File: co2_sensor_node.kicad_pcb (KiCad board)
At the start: 4 copper layers, 100 x 100 mm, 132 parts, among them J1 Conn_01x03, J10 Conn_01x04, J11 USB_B, J12 Conn_01x02, J13 TF-15x15, J2 Conn_01x03, J3 Conn_01x02, J4 Conn_01x02, J5 Conn_01x03, J6 Conn_01x03, J7 Conn_01x02, J8 Conn_01x02, J9 Conn_01x04, Q1 AO3400A, Q2 AO3401A, Q3 AO3401A, Q4 SS8050, Q5 SS8050, Q6 AO3400A, SW1 K2-1102SP-C4SC-04, U1 BQ24074RGT, U2 TPS62130, U3 CH340C, U4 ESP32-WROOM-32D, U5 TC1508S

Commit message: Add 5V boost converter and begin redesign of PCB
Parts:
- removed the J1 at (114.0, 103.5)
- removed the J11 at (175.2, 67.1)
- removed J12: Conn_01x02, co2_sensor_node:KF301-5.0-2P
- removed the J2 at (114.0, 86.3)
- removed the JP2 at (166.0, 61.5)
- removed kibuzzard-628D00BE: G***, kibuzzard-628D00BE
- removed kibuzzard-6294C7F1: G***, kibuzzard-6294C7F1
- removed kibuzzard-6294C850: G***, kibuzzard-6294C850
- removed kibuzzard-6294C860: G***, kibuzzard-6294C860
- added C1: 22n, Capacitor_SMD:C_0603_1608Metric, F.Cu at (275.6, 19.2)
- added C17: 1u, Capacitor_SMD:C_0603_1608Metric, F.Cu at (368.5, 123.2)
- added C2: 100n, Capacitor_SMD:C_0603_1608Metric, F.Cu at (275.6, 21.7)
- added C3: 22u, Capacitor_SMD:C_0805_2012Metric, F.Cu at (267.4, 24.8)
- added C4: 1n8, Capacitor_SMD:C_0603_1608Metric, F.Cu at (268.0, 27.6)
- added C5: 100n, Capacitor_SMD:C_0603_1608Metric, F.Cu at (271.6, 24.6)
- added C6: 10u, Capacitor_SMD:C_0805_2012Metric, F.Cu at (263.8, 27.8)
- added C7: 10u, Capacitor_SMD:C_0805_2012Metric, F.Cu at (275.8, 16.4)
- added C8: 10u, Capacitor_SMD:C_0805_2012Metric, F.Cu at (259.3, 27.8)
- added D2: SS34, Diode_SMD:D_SMA, F.Cu at (261.1, 24.0)
- added J8: Conn_01x04, Connector_JST:JST_XH_B4B-XH-A_1x04_P2.50mm_Vertical, F.Cu at (331.5, 100.0)
- added J9: Conn_01x04_Male, Connector_PinHeader_2.54mm:PinHeader_1x04_P2.54mm_Vertical, F.Cu at (361.2, 128.9)
- added L1: 2u7, co2_sensor_node:PCD0504MT2R7, F.Cu at (269.8, 17.2)
- added R10: 30k5, Resistor_SMD:R_0402_1005Metric, F.Cu at (271.5, 26.8)
- added R11: 10k, Resistor_SMD:R_0603_1608Metric, F.Cu at (280.0, 16.2)
- added R4: 60k4, Resistor_SMD:R_0402_1005Metric, F.Cu at (279.5, 18.4)
- added R5: 866, Resistor_SMD:R_0402_1005Metric, F.Cu at (275.1, 24.0)
- added U1: TPS55340PWP, Package_SO:HTSSOP-14-1EP_4.4x5mm_P0.65mm_EP3.4x5mm_Mask3x3.1mm_ThermalVias, F.Cu at (261.5, 18.3)
- added kibuzzard-628D076D: G***, kibuzzard-628D076D, F.Cu at (360.0, 73.8)
- added kibuzzard-628D0781: G***, kibuzzard-628D0781, F.Cu at (357.8, 73.8)
- added kibuzzard-62D933FC: G***, kibuzzard-62D933FC, F.Cu at (359.0, 64.0)
- added kibuzzard-62D936A1: G***, kibuzzard-62D936A1, F.Cu at (358.2, 127.2)
- added kibuzzard-62D936BA: G***, kibuzzard-62D936BA, F.Cu at (358.2, 130.7)
- added kibuzzard-62D936C1: G***, kibuzzard-62D936C1, F.Cu at (358.2, 134.0)
- added kibuzzard-62D936C8: G***, kibuzzard-62D936C8, F.Cu at (358.2, 138.0)
- added kibuzzard-62D936D1: G***, kibuzzard-62D936D1, F.Cu at (355.5, 132.5)
- added kibuzzard-62D95196: G***, kibuzzard-62D95196, F.Cu at (347.8, 119.0)
- J10: value Conn_01x04 -> Conn_01x02; footprint Connector_JST:JST_XH_B4B-XH-A_1x04_P2.50mm_Vertical -> Connector_JST:JST_XH_B2B-XH-AM_1x02_P2.50mm_Vertical
- moved TP17 228.7 mm to (331.5, 83.5), turned to 180 degrees
- moved TP15 228.1 mm to (331.5, 87.0), turned to 180 degrees
- moved TP14 227.8 mm to (331.5, 90.5), turned to 180 degrees
- moved TP16 227.7 mm to (331.5, 94.0), turned to 180 degrees
- moved D3 224.1 mm to (348.2, 64.2), turned to 180 degrees
- moved TP10 220.4 mm to (325.0, 115.8)
- moved R18 219.4 mm to (345.7, 66.2), turned to 180 degrees
- moved Q3 219.3 mm to (347.2, 60.9), turned to 90 degrees
- moved TP13 217.2 mm to (324.8, 108.5)
- moved TP12 217.1 mm to (324.8, 125.5)
- moved C22 216.7 mm to (326.6, 81.0), turned to 180 degrees
- moved C23 216.4 mm to (326.7, 82.8), turned to 180 degrees
- moved J10 214.7 mm to (344.5, 113.5)
- moved kibuzzard-628D06EC 212.6 mm to (337.0, 57.2), turned to 0 degrees
- moved F1 211.3 mm to (343.2, 62.1), turned to -90 degrees
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- renumbered C2 to C10, C3 to C11, C4 to C12, C5 to C13, C6 to C14, C7 to C15, C8 to C16, C9 to C18, C10 to C19, C11 to C20, C12 to C21, C13 to C22, C14 to C23, C1 to C9, D2 to D3, D3 to D4, J3 to J1, J13 to J11, J4 to J2, J5 to J3, J6 to J4, J7 to J5, J8 to J6, J9 to J7, JP3 to JP2, L1 to L2, R11 to R12, R7 to R13, R9 to R14, R10 to R15, R12 to R16, R13 to R17, R14 to R18, R15 to R19, R16 to R20, R17 to R21, R18 to R22, R19 to R23, R20 to R24, R21 to R25, R4 to R6, R5 to R7, R6 to R8, R8 to R9, U1 to U2, U2 to U3, U3 to U4, U4 to U5, U5 to U6
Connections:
- C22 pad 1: /Atmo sensor/3V3_IN -> /Power/3V3_switch
- C23 pad 1: /Atmo sensor/3V3_IN -> /Power/3V3_switch
- D4 pad 1: /Atmo sensor/3V3_IN -> /Power/3V3_switch
- D4 pad 2: Net-(D3-Pad2) (its old number) -> Net-(D4-Pad2)
- J10 pad 1: /Atmo sensor/3V3_IN -> Net-(D4-Pad2)
- J10 pad 2: /Atmo sensor/SCL -> /Power/3V3_switch
- J11 pad 4: /Atmo sensor/3V3_IN -> /Power/3V3_switch
- J3 pad 1: /Atmo sensor/3V3_IN -> /Power/3V3_switch
- J4 pad 1: /Atmo sensor/3V3_IN -> /Power/3V3_switch
- J7 pad 3: /Atmo sensor/3V3_IN -> /Power/3V3_switch
- Q2 pad 3: /Atmo sensor/3V3_IN -> /Power/3V3_switch
- Q6 pad 3: Net-(D3-Pad2) (its old number) -> Net-(D4-Pad2)
- R1 pad 2: /Atmo sensor/3V3_IN -> /Power/3V3_switch
- R2 pad 2: /Atmo sensor/3V3_IN -> /Power/3V3_switch
- R25 pad 1: /Atmo sensor/3V3_IN -> /Power/3V3_switch
- TP1 pad 1: /Atmo sensor/3V3_IN -> /Power/3V3_switch
- U6 pad 4: /Atmo sensor/3V3_IN -> /Power/3V3_switch
- U6 pad 8: /Atmo sensor/3V3_IN -> /Power/3V3_switch
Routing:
- net /Atmo sensor/3V3_IN: track 275.5 -> 0.00 mm, vias 4 -> 0
- net /Microprocessor section/VALVE_2_REV: track 141.7 -> 6.62 mm
- net /Microprocessor section/VALVE_2_FWD: track 140.3 -> 5.84 mm
- net /Microprocessor section/VALVE_1_FWD: track 140.6 -> 6.66 mm
- net /Microprocessor section/VALVE_1_REV: track 138.7 -> 5.85 mm
- net /Microprocessor section/MOISTURE_SENSOR: track 127.2 -> 13.0 mm
- net /Microprocessor section/TEMP_SENSOR: track 118.9 -> 13.4 mm
- net +3V3: track 92.6 -> 13.1 mm, vias 5 -> 4
- net /Atmo sensor/SCL: track 84.4 -> 18.1 mm
- net /Atmo sensor/SDA: track 74.6 -> 21.9 mm
- net /Microprocessor section/SPI_SD_CSN: track 52.6 -> 9.89 mm
- net /Microprocessor section/SPI_MOSI: track 47.6 -> 9.43 mm
- net /Microprocessor section/SPI_SCLK: track 37.3 -> 7.17 mm
- net /Microprocessor section/PWR_EN: track 31.3 -> 2.78 mm, vias 1 -> 0
- net /Microprocessor section/SPI_MISO: track 36.9 -> 10.1 mm
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- added copper zone on F.Cu, net +BATT
- added copper zone on F.Cu, net /Power/PWR_OUT
- added copper zone on F.Cu, net Net-(D2-Pad2)
- added copper zone on F.Cu, net Net-(J5-Pad2)
- removed copper zone on F.Cu, net /Atmo sensor/3V3_IN
- removed copper zone on F.Cu, net Net-(F1-Pad2)
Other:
- board size 100 x 100 mm -> 77.5 x 100 mm
- board text added: "GND"

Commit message: More layout work
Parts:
- moved SW1 108.8 mm to (267.2, 41.5)
- moved C23 101.5 mm to (225.2, 79.8)
- moved C10 101.5 mm to (256.0, 75.2)
- moved C11 101.5 mm to (260.2, 73.0)
- moved C12 101.5 mm to (262.0, 73.0)
- moved C13 101.5 mm to (256.0, 78.8)
- moved C14 101.5 mm to (254.0, 78.8)
- moved C15 101.5 mm to (252.0, 78.8)
- moved C16 101.5 mm to (250.0, 78.8)
- moved C17 101.5 mm to (267.0, 120.2)
- moved C18 101.5 mm to (274.5, 87.0)
- moved C19 101.5 mm to (278.2, 82.3)
- moved C20 101.5 mm to (274.5, 89.5)
- moved C21 101.5 mm to (274.5, 91.2)
- moved C22 101.5 mm to (225.1, 78.0)
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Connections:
- C22 pad 1: /Power/3V3_switch -> +5V
- C23 pad 1: /Power/3V3_switch -> +5V
- U6 pad 4: /Power/3V3_switch -> +5V
- U6 pad 8: /Power/3V3_switch -> +5V
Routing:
- net GND: track 74.9 -> 21.1 mm, vias 21 -> 6
- net /Microprocessor section/EN: track 22.6 -> 0.00 mm
- net /Atmo sensor/SDA: track 21.9 -> 0.00 mm, vias 1 -> 0
- net /Fan/FAN: track 21.1 -> 0.00 mm
- net Net-(J9-Pad3): track 20.1 -> 0.00 mm
- net Net-(J9-Pad2): track 19.9 -> 0.00 mm
- net /Atmo sensor/SCL: track 18.1 -> 0.00 mm, vias 1 -> 0
- net /Microprocessor section/TEMP_SENSOR: track 13.4 -> 0.00 mm, vias 1 -> 0
- net /CO2 Sensor Connector/UART_RX: track 13.1 -> 0.00 mm
- net /Microprocessor section/MOISTURE_SENSOR: track 13.0 -> 0.00 mm, vias 1 -> 0
- net +3V3: track 13.1 -> 0.07 mm, vias 4 -> 0
- net /Power/PWR_OUT: track 11.2 -> 0.00 mm
- net /Valve Driver/OUT_D: track 10.7 -> 0.00 mm
- net /Valve Driver/OUT_A: track 10.7 -> 0.00 mm
- net /Valve Driver/OUT_C: track 10.2 -> 0.00 mm
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- removed copper zone on F.Cu, net +3V3
- removed copper zone on F.Cu, net +BATT
- removed copper zone on F.Cu, net /Power/PWR_OUT
- removed copper zone on F.Cu, net GND
- removed copper zone on F.Cu, net Net-(D2-Pad2)
- removed copper zone on F.Cu, net Net-(F1-Pad1)
- removed copper zone on F.Cu, net Net-(J5-Pad2)
- removed copper zone on F.Cu, net Net-(L2-Pad1)

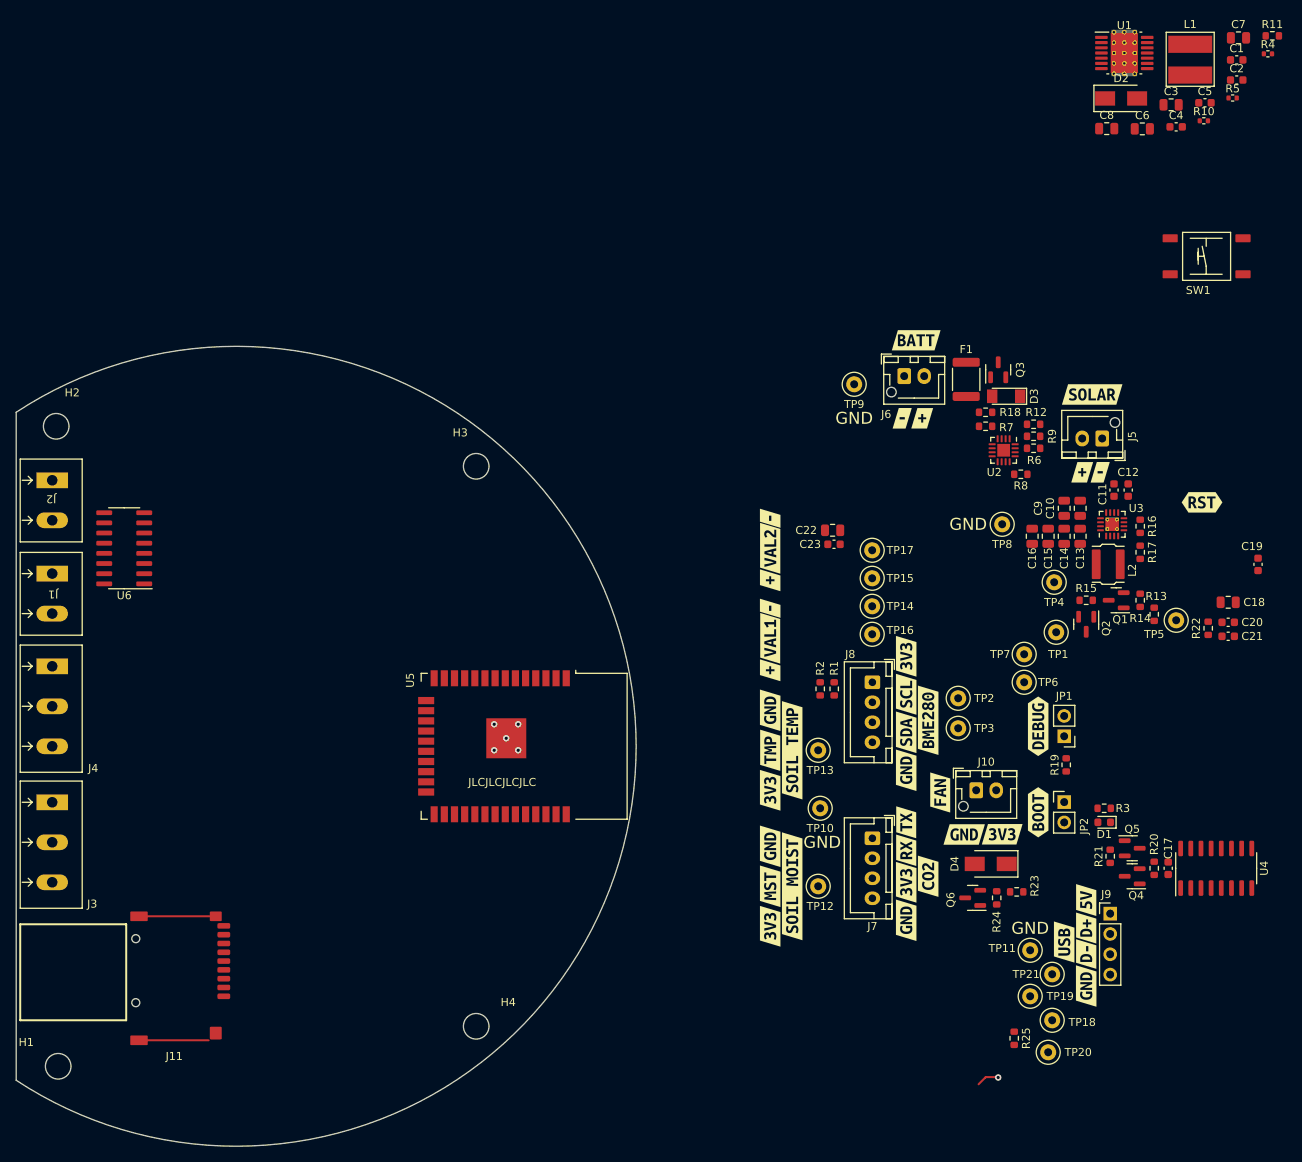
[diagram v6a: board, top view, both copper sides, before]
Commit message: Finish component placement
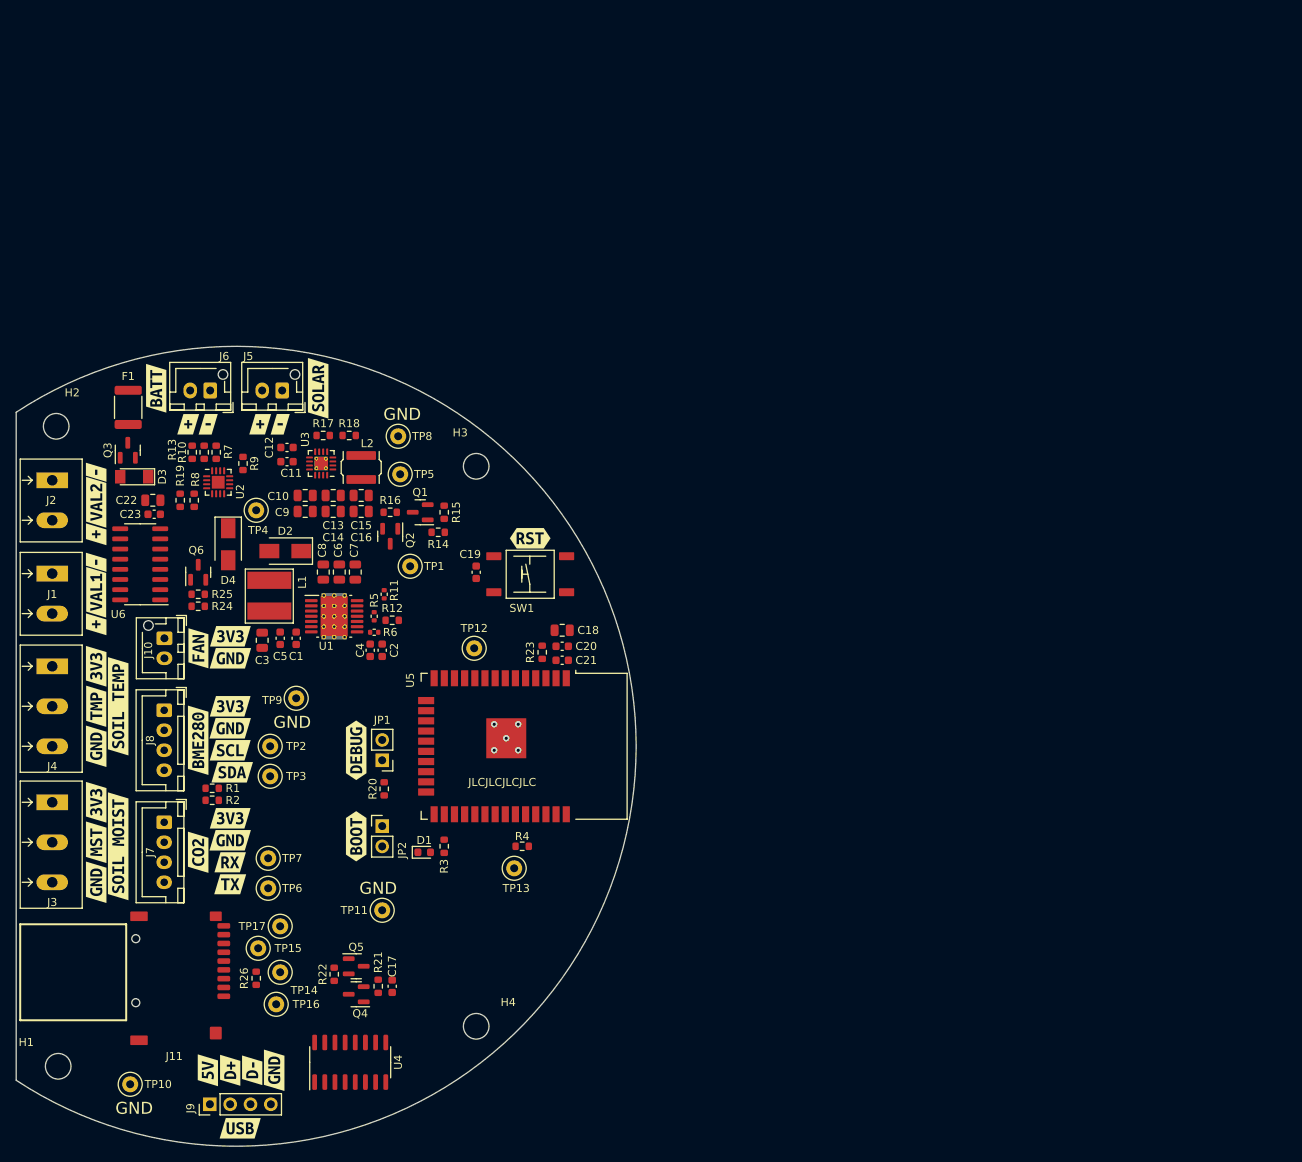
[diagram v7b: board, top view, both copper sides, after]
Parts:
- removed the TP14 at (230.0, 87.5)
- removed the TP15 at (230.0, 84.0)
- removed the TP16 at (230.0, 91.0)
- removed the TP17 at (230.0, 80.5)
- removed the TP5 at (268.0, 89.2)
- added R4: 4k7, Resistor_SMD:R_0603_1608Metric, F.Cu at (186.2, 117.5)
- added TP4: 5V, TestPoint:TestPoint_Loop_D2.50mm_Drill1.0mm_LowProfile, F.Cu at (153.0, 75.5)
- moved C1 138.0 mm to (158.0, 91.5), turned to -90 degrees
- moved L1 135.2 mm to (154.6, 88.1), turned to 180 degrees
- moved C5 133.6 mm to (156.0, 91.5), turned to -90 degrees
- moved R12 132.1 mm to (170.0, 89.2), turned to 180 degrees
- moved R5 132.0 mm to (167.8, 88.8), turned to 90 degrees
- moved C3 131.9 mm to (153.8, 91.8), turned to -90 degrees
- moved C7 129.0 mm to (165.4, 83.2), turned to -90 degrees
- moved C2 128.4 mm to (168.8, 93.0), turned to -90 degrees
- moved R6 126.4 mm to (167.8, 90.8), turned to 180 degrees
- moved U1 121.3 mm to (162.8, 88.8)
- moved C4 120.1 mm to (167.2, 93.0), turned to -90 degrees
- moved D2 118.8 mm to (156.6, 80.6), turned to 180 degrees
- moved R11 118.3 mm to (169.0, 86.0), turned to -90 degrees
- moved J9 115.0 mm to (147.2, 149.8), turned to 90 degrees
- moved C6 114.7 mm to (163.4, 83.2), turned to -90 degrees
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- renumbered R9 to R10, R10 to R11, R11 to R12, R12 to R13, R13 to R14, R14 to R15, R15 to R16, R16 to R17, R17 to R18, R18 to R19, R19 to R20, R20 to R21, R21 to R22, R22 to R23, R23 to R24, R24 to R25, R25 to R26, R4 to R5, R5 to R6, R6 to R7, R7 to R8, R8 to R9, TP18 to TP14, TP19 to TP15, TP20 to TP16, TP21 to TP17, TP4 to TP5
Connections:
- D4 pad 1: /Power/3V3_switch -> +5V
- J10 pad 1: Net-(D4-Pad2) -> +5V
- J10 pad 2: /Power/3V3_switch -> Net-(D4-Pad2)
- J7 pad 1: /CO2 Sensor Connector/UART_TX -> /Power/3V3_switch
- J7 pad 2: /CO2 Sensor Connector/UART_RX -> GND
- J7 pad 3: /Power/3V3_switch -> /CO2 Sensor Connector/UART_RX
- J7 pad 4: GND -> /CO2 Sensor Connector/UART_TX
- J8 pad 2: /Atmo sensor/SCL -> GND
- J8 pad 3: /Atmo sensor/SDA -> /Atmo sensor/SCL
- J8 pad 4: GND -> /Atmo sensor/SDA
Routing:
- net GND: track 21.1 -> 0.00 mm, vias 6 -> 5
